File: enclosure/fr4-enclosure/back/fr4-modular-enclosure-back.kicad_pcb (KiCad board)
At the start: 2 copper layers, 256 x 320 mm, 0 parts

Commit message: Fixed FR4 enclosure panels
There was an inconsistent behavior on the gerber viewer of JLCPCB. Added a layer of GND to all panels with a plated mounting hole that allows full isolation (Faraday-cage) of the enclosure, to minimize noise.
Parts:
- added H1: MountingHole_Pad, MountingHole:MountingHole_3.2mm_M3_Pad_TopOnly, B.Cu at (128.0, 160.0)
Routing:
- added copper zone on B.Cu, net GND
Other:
- outline, holes or cut-outs redrawn

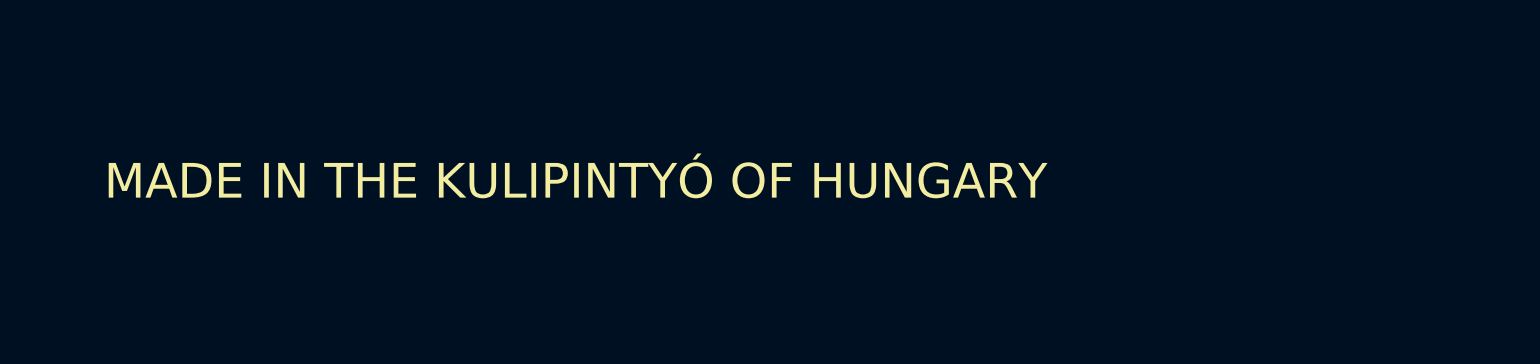
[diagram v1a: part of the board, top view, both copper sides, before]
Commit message: Added FR4 enclosure files
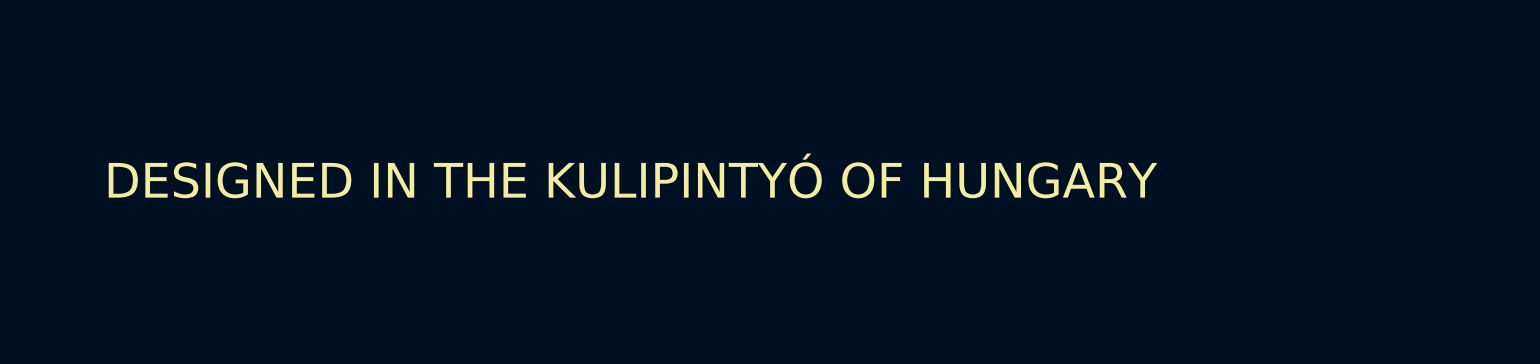
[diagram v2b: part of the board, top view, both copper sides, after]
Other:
- board text added: "DESIGNED IN THE KULIPINTYÓ OF HUNGARY"
- board text removed: "MADE IN THE KULIPINTYÓ OF HUNGARY"
